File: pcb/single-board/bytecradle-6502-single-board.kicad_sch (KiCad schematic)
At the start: 36 parts, among them J1 USB_B, J2 EXPBUS1, J3 EXPBUS2, SW1 SW_SPDT, SW2 RESET, SW3 NMI, U1 74AC14, U2 W65C02, U3 CD74HC688, U4 74AC08, X1 14 MHz

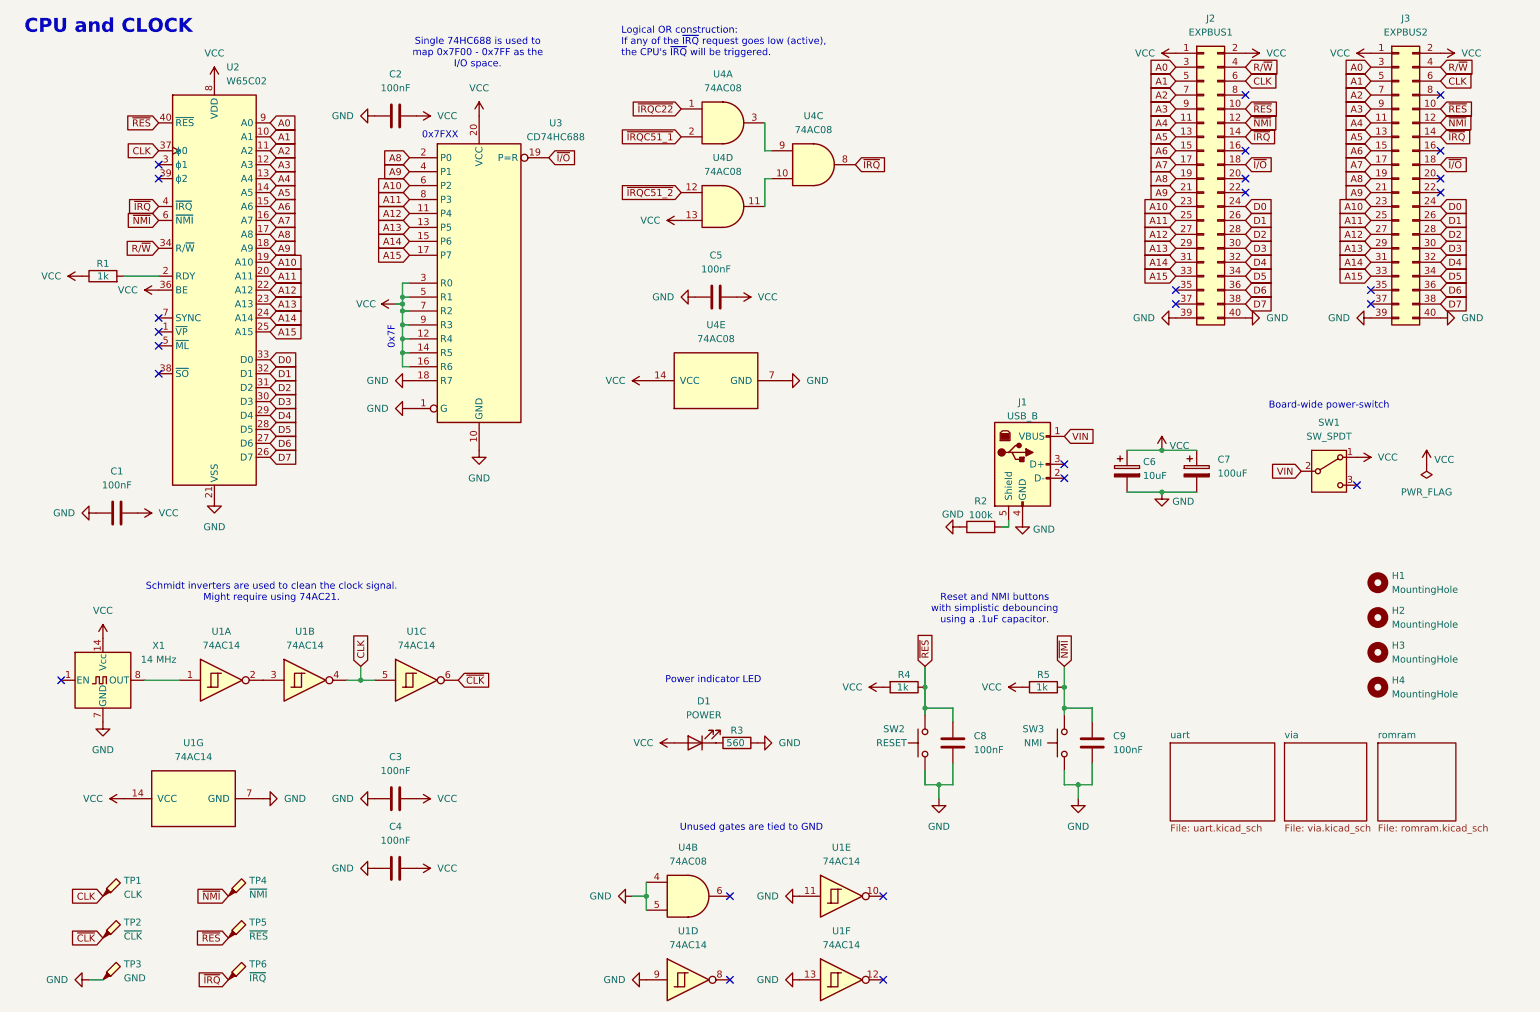
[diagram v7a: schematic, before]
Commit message: Revising single board layout
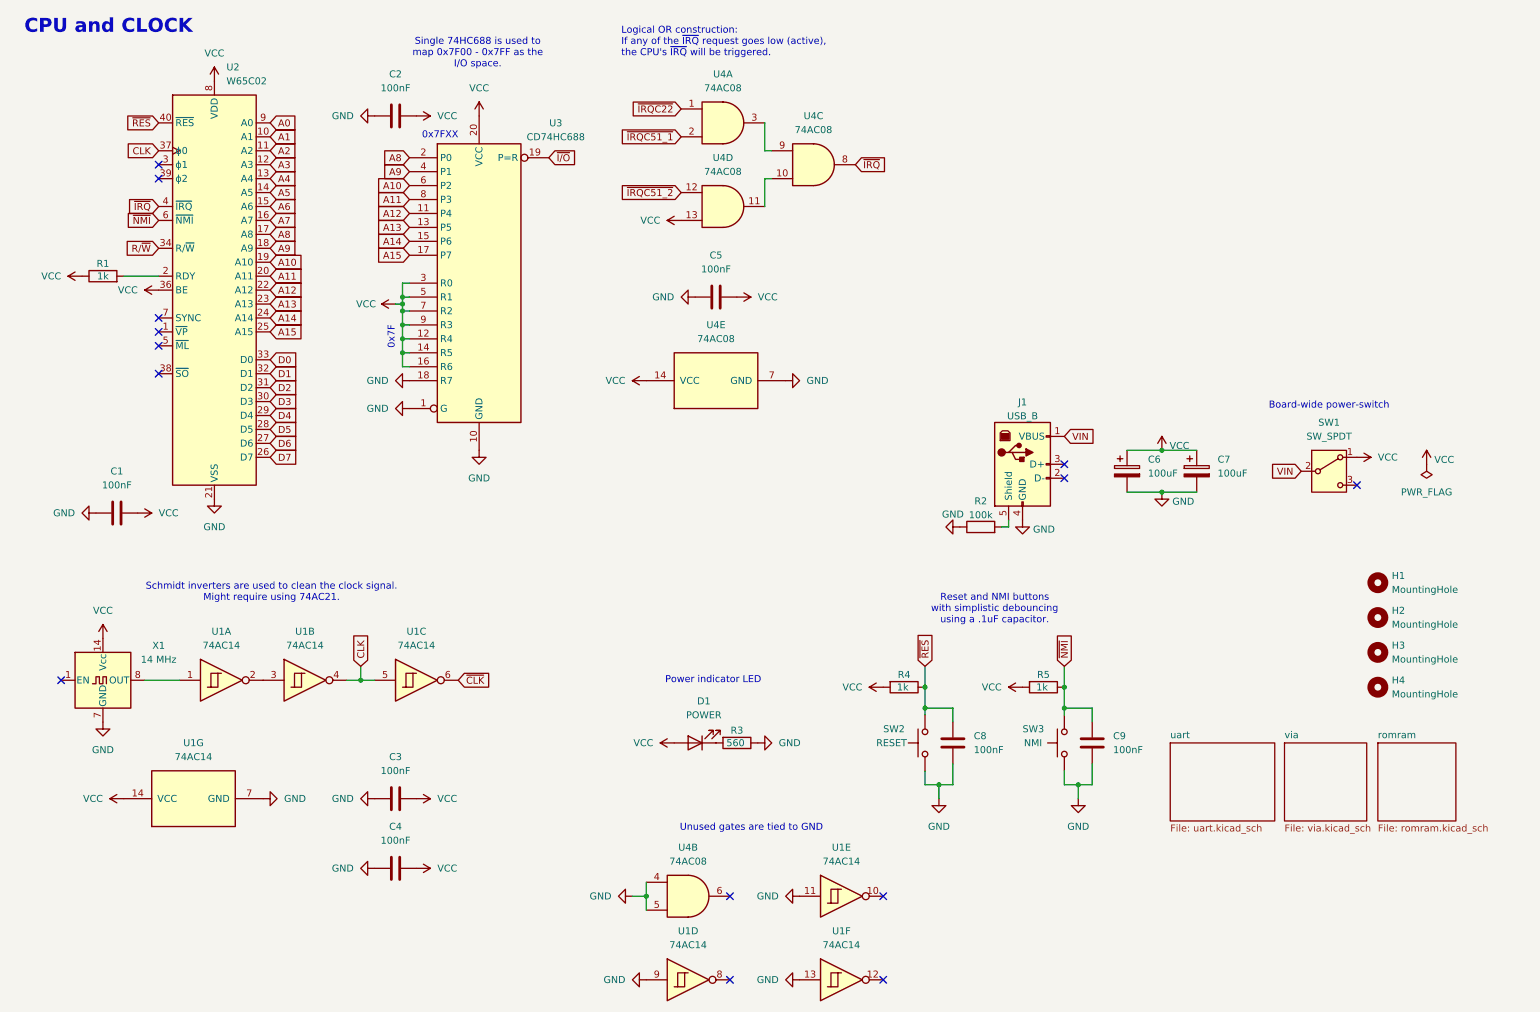
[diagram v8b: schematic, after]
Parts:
- removed J2: EXPBUS1, Connector_PinHeader_2.54mm:PinHeader_2x20_P2.54mm_Vertical, symbol Connector_Generic:Conn_02x20_Odd_Even
- removed J3: EXPBUS2, Connector_PinHeader_2.54mm:PinHeader_2x20_P2.54mm_Vertical, symbol Connector_Generic:Conn_02x20_Odd_Even
- removed TP1: CLK, Connector_PinHeader_2.54mm:PinHeader_1x01_P2.54mm_Vertical, symbol Connector:TestPoint_Probe
- removed TP2: ~{CLK}, Connector_PinHeader_2.54mm:PinHeader_1x01_P2.54mm_Vertical, symbol Connector:TestPoint_Probe
- removed TP3: GND, Connector_PinHeader_2.54mm:PinHeader_1x01_P2.54mm_Vertical, symbol Connector:TestPoint_Probe
- removed TP4: ~{NMI}, Connector_PinHeader_2.54mm:PinHeader_1x01_P2.54mm_Vertical, symbol Connector:TestPoint_Probe
- removed TP5: ~{RES}, Connector_PinHeader_2.54mm:PinHeader_1x01_P2.54mm_Vertical, symbol Connector:TestPoint_Probe
- removed TP6: ~{IRQ}, Connector_PinHeader_2.54mm:PinHeader_1x01_P2.54mm_Vertical, symbol Connector:TestPoint_Probe
- C6: value 10uF -> 100uF
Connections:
- no-connect marks 26 -> 14
